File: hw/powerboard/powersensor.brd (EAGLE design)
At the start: 26.3 x 31.1 mm, 35 parts, among them J1 ISP, J2 I2C

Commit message: Added optional I2C pullups, broke out PB0/1 and performed some cosmetical changes to PowerSensor board
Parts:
- added R17, R18: (no value), SparkFun-Passives:0603-RES
- J8: device SparkFun-Connectors:1X04 -> SparkFun-Connectors:1X06
- R1: value (none) -> 12k9
- R10, R11, R2, R5, R8: value (none) -> 1k1
- R4: value (none) -> 4k9
- R7: value (none) -> 2k9
- moved C5 0.16 mm to (8.57, 5.87)
- moved J2 0.16 mm to (1.43, 10.8)
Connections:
- new net PB0: J8.5, U$1.2
- new net PB1: J8.4, U$1.3
- net SCK: now also R17.2
- net SDA/MOSI: now also R18.1
- net VIN: now also J8.6, R17.1, R18.2; no longer J8.4
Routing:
- net PB0: track 0.00 -> 5.35 mm
- net PB1: track 0.00 -> 4.82 mm
- net SDA/MOSI: track 21.3 -> 24.4 mm
- net SCK: track 18.8 -> 21.9 mm
- net VIN: track 29.6 -> 31.8 mm
- net MISO/1.8V_ADC: track 10.1 -> 10.7 mm
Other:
- board text added: "I2C pullups"
- board text added: "MISO"
- board text added: "MOSI"
- board text added: "PB0"
- board text added: "PB1"
- board text added: "PowerSensor v0.1"
- board text added: "RST"
- board text removed: "BIVAC PowerSensor v0.1"

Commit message: Added values and performed some cosmetic changes on PowerSensor schematics
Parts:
- C1, C2, C3, C4: value (none) -> 10u
- R1: value 12k9 -> 13k
- R12, R3, R6, R9: value (none) -> 750R
- R17, R18: value (none) -> 4k7
- R4: value 4k9 -> 4k87
- R7: value 2k9 -> 2k87
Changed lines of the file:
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@@
 </autorouter>
 <elements>
-<element name="C1" library="SparkFun-Capacitors" package="0603-CAP" value="" x="8.89" y="17.78" rot="R90"/>
-<element name="C2" library="SparkFun-Capacitors" package="0603-CAP" value="" x="13.97" y="17.78" rot="R90"/>
-<element name="C3" library="SparkFun-Capacitors" package="0603-CAP" value="" x="19.05" y="17.78" rot="R90"/>
-<element name="C4" library="SparkFun-Capacitors" package="0603-CAP" value="" x="24.13" y="17.78" rot="R90"/>
+<element name="C1" library="SparkFun-Capacitors" package="0603-CAP" value="10u" x="8.89" y="17.78" rot="R90"/>
+<element name="C2" library="SparkFun-Capacitors" package="0603-CAP" value="10u" x="13.97" y="17.78" rot="R90"/>
+<element name="C3" library="SparkFun-Capacitors" package="0603-CAP" value="10u" x="19.05" y="17.78" rot="R90"/>
+<element name="C4" library="SparkFun-Capacitors" package="0603-CAP" value="10u" x="24.13" y="17.78" rot="R90"/>
 <element name="C5" library="SparkFun-Capacitors" package="0603-CAP" value="100nF" x="8.5725" y="5.87375" smashed="yes" rot="R180">
 <attribute name="NAME" x="10.12825" y="6.2865" size="0.4064" layer="25" font="vector" rot="R270"/>
@@
 <attribute name="VALUE" x="18.415" y="29.845" size="1.27" layer="27" rot="R270"/>
 </element>
-<element name="R1" library="SparkFun-Passives" package="0603-RES" value="12k9" x="6.35" y="21.59" rot="R90"/>
+<element name="R1" library="SparkFun-Passives" package="0603-RES" value="13k" x="6.35" y="21.59" rot="R90"/>
 <element name="R10" library="SparkFun-Passives" package="0603-RES" value="1k1" x="21.59" y="21.59" rot="R90"/>
 <element name="R11" library="SparkFun-Passives" package="0603-RES" value="1k1" x="24.13" y="21.59" rot="R270"/>
-<element name="R12" library="SparkFun-Passives" package="0603-RES" value="" x="21.59" y="17.78" rot="R90"/>
+<element name="R12" library="SparkFun-Passives" package="0603-RES" value="750R" x="21.59" y="17.78" rot="R90"/>
 <element name="R13" library="SparkFun-Passives" package="0603-RES" value="" x="8.89" y="28.575" smashed="yes" rot="R270">
 <attribute name="NAME" x="9.4615" y="30.6705" size="0.4064" layer="25" font="vector" rot="R180"/>
@@
 </element>
 <element name="R2" library="SparkFun-Passives" package="0603-RES" value="1k1" x="8.89" y="21.59" rot="R270"/>
-<element name="R3" library="SparkFun-Passives" package="0603-RES" value="" x="6.35" y="17.78" rot="R90"/>
-<element name="R4" library="SparkFun-Passives" package="0603-RES" value="4k9" x="11.43" y="21.59" smashed="yes" rot="R90">
+<element name="R3" library="SparkFun-Passives" package="0603-RES" value="750R" x="6.35" y="17.78" rot="R90"/>
+<element name="R4" library="SparkFun-Passives" package="0603-RES" value="4k87" x="11.43" y="21.59" smashed="yes" rot="R90">
 <attribute name="NAME" x="10.668" y="20.701" size="0.4064" layer="25" font="vector" rot="R90"/>
 <attribute name="VALUE" x="12.573" y="20.574" size="0.4064" layer="27" font="vector" rot="R90"/>
 </element>
 <element name="R5" library="SparkFun-Passives" package="0603-RES" value="1k1" x="13.97" y="21.59" rot="R270"/>
-<element name="R6" library="SparkFun-Passives" package="0603-RES" value="" x="11.43" y="17.78" rot="R90"/>
-<element name="R7" library="SparkFun-Passives" package="0603-RES" value="2k9" x="16.51" y="21.59" rot="R90"/>
+<element name="R6" library="SparkFun-Passives" package="0603-RES" value="750R" x="11.43" y="17.78" rot="R90"/>
+<element name="R7" library="SparkFun-Passives" package="0603-RES" value="2k87" x="16.51" y="21.59" rot="R90"/>
 <element name="R8" library="SparkFun-Passives" package="0603-RES" value="1k1" x="19.05" y="21.59" rot="R270"/>
-<element name="R9" library="SparkFun-Passives" package="0603-RES" value="" x="16.51" y="17.78" rot="R90"/>
+<element name="R9" library="SparkFun-Passives" package="0603-RES" value="750R" x="16.51" y="17.78" rot="R90"/>
 <element name="U$1" library="SparkFun-DigitalIC" package="SO14" value="ATTINY84" x="13.335" y="10.795" smashed="yes">
 <attribute name="PROD_ID" value="IC-11285" x="13.335" y="10.795" size="1.778" layer="27" display="off"/>
@@
 <attribute name="VALUE" x="1.905" y="0" size="1.27" layer="27"/>
 </element>
-<element name="R17" library="SparkFun-Passives" package="0603-RES" value="" x="9.04875" y="10.795" rot="MR0"/>
-<element name="R18" library="SparkFun-Passives" package="0603-RES" value="" x="9.04875" y="8.255" rot="MR180"/>
+<element name="R17" library="SparkFun-Passives" package="0603-RES" value="4k7" x="9.04875" y="10.795" rot="MR0"/>
+<element name="R18" library="SparkFun-Passives" package="0603-RES" value="4k7" x="9.04875" y="8.255" rot="MR180"/>
 </elements>
 <signals>

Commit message: Fixed values and added product ids for PowerSensor BOM
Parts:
- R13: value (none) -> 560R
- R14: value (none) -> 180R
- R15: value (none) -> 82R
- R16: value (none) -> 0R
- R4: value 4k87 -> 4k7
- R7: value 2k87 -> 2k7
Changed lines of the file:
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@@
 <element name="R11" library="SparkFun-Passives" package="0603-RES" value="1k1" x="24.13" y="21.59" rot="R270"/>
 <element name="R12" library="SparkFun-Passives" package="0603-RES" value="750R" x="21.59" y="17.78" rot="R90"/>
-<element name="R13" library="SparkFun-Passives" package="0603-RES" value="" x="8.89" y="28.575" smashed="yes" rot="R270">
+<element name="R13" library="SparkFun-Passives" package="0603-RES" value="560R" x="8.89" y="28.575" smashed="yes" rot="R270">
 <attribute name="NAME" x="9.4615" y="30.6705" size="0.4064" layer="25" font="vector" rot="R180"/>
 <attribute name="VALUE" x="7.747" y="29.591" size="0.4064" layer="27" font="vector" rot="R270"/>
 </element>
-<element name="R14" library="SparkFun-Passives" package="0603-RES" value="" x="13.97" y="28.575" smashed="yes" rot="R270">
+<element name="R14" library="SparkFun-Passives" package="0603-RES" value="180R" x="13.97" y="28.575" smashed="yes" rot="R270">
 <attribute name="NAME" x="14.5415" y="30.6705" size="0.4064" layer="25" font="vector" rot="R180"/>
 <attribute name="VALUE" x="12.827" y="29.591" size="0.4064" layer="27" font="vector" rot="R270"/>
 </element>
-<element name="R15" library="SparkFun-Passives" package="0603-RES" value="" x="19.05" y="28.575" smashed="yes" rot="R270">
+<element name="R15" library="SparkFun-Passives" package="0603-RES" value="82R" x="19.05" y="28.575" smashed="yes" rot="R270">
 <attribute name="NAME" x="19.6215" y="30.6705" size="0.4064" layer="25" font="vector" rot="R180"/>
 <attribute name="VALUE" x="17.907" y="29.591" size="0.4064" layer="27" font="vector" rot="R270"/>
 </element>
-<element name="R16" library="SparkFun-Passives" package="0603-RES" value="" x="24.13" y="28.575" smashed="yes" rot="R270">
+<element name="R16" library="SparkFun-Passives" package="0603-RES" value="0R" x="24.13" y="28.575" smashed="yes" rot="R270">
 <attribute name="NAME" x="24.7015" y="30.6705" size="0.4064" layer="25" font="vector" rot="R180"/>
 <attribute name="VALUE" x="22.987" y="29.591" size="0.4064" layer="27" font="vector" rot="R270"/>
@@
 <element name="R2" library="SparkFun-Passives" package="0603-RES" value="1k1" x="8.89" y="21.59" rot="R270"/>
 <element name="R3" library="SparkFun-Passives" package="0603-RES" value="750R" x="6.35" y="17.78" rot="R90"/>
-<element name="R4" library="SparkFun-Passives" package="0603-RES" value="4k87" x="11.43" y="21.59" smashed="yes" rot="R90">
+<element name="R4" library="SparkFun-Passives" package="0603-RES" value="4k7" x="11.43" y="21.59" smashed="yes" rot="R90">
 <attribute name="NAME" x="10.668" y="20.701" size="0.4064" layer="25" font="vector" rot="R90"/>
 <attribute name="VALUE" x="12.573" y="20.574" size="0.4064" layer="27" font="vector" rot="R90"/>
@@
 <element name="R5" library="SparkFun-Passives" package="0603-RES" value="1k1" x="13.97" y="21.59" rot="R270"/>
 <element name="R6" library="SparkFun-Passives" package="0603-RES" value="750R" x="11.43" y="17.78" rot="R90"/>
-<element name="R7" library="SparkFun-Passives" package="0603-RES" value="2k87" x="16.51" y="21.59" rot="R90"/>
+<element name="R7" library="SparkFun-Passives" package="0603-RES" value="2k7" x="16.51" y="21.59" rot="R90"/>
 <element name="R8" library="SparkFun-Passives" package="0603-RES" value="1k1" x="19.05" y="21.59" rot="R270"/>
 <element name="R9" library="SparkFun-Passives" package="0603-RES" value="750R" x="16.51" y="17.78" rot="R90"/>

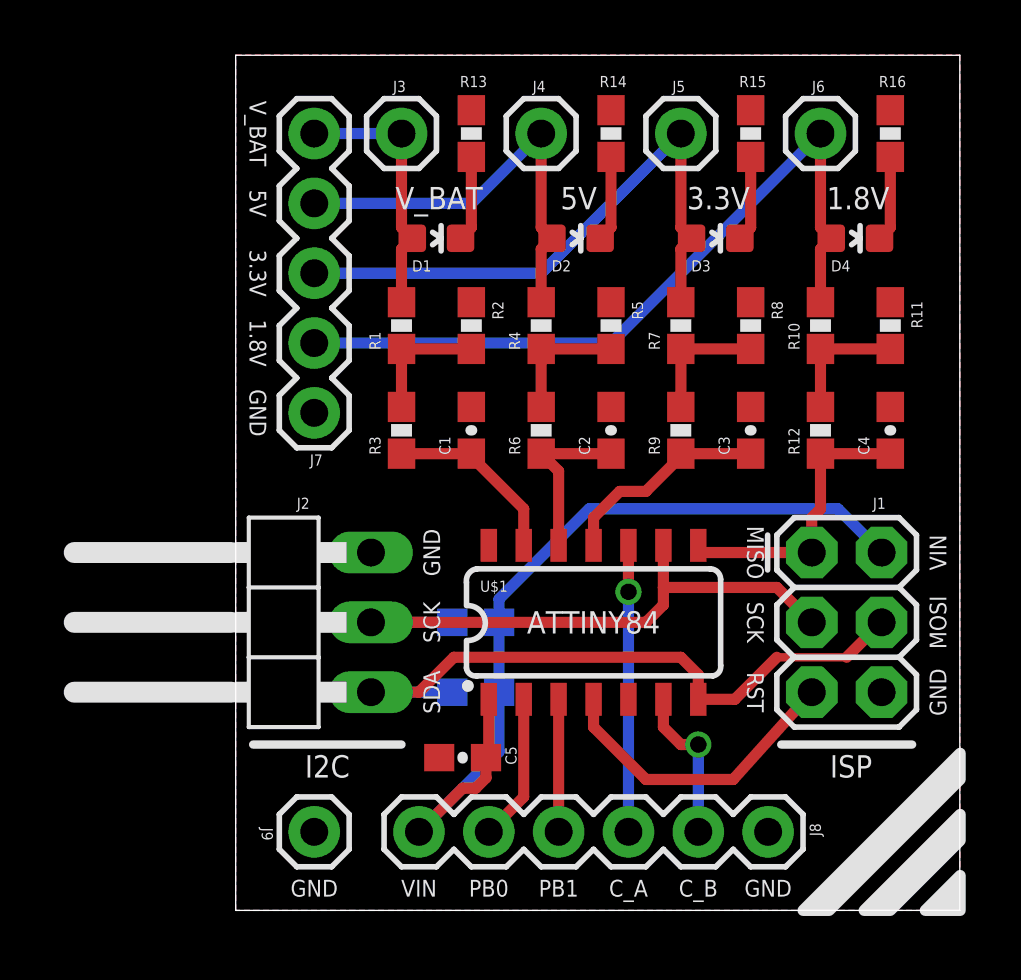
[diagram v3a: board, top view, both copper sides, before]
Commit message: Added PowerSensor package to custom library
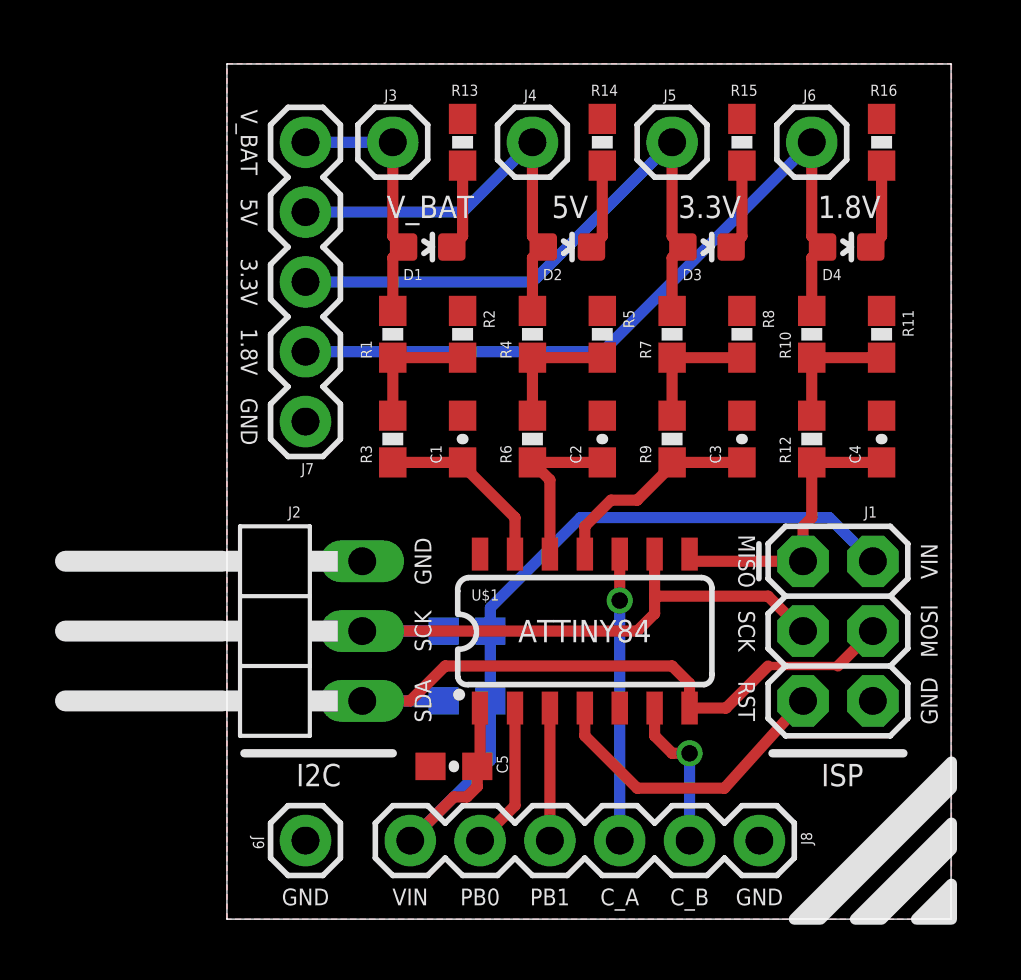
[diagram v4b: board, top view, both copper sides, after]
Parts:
- moved R9 0.45 mm to (16.2, 17.5)
- moved C1 0.45 mm to (8.57, 17.5)
- moved C2 0.45 mm to (13.7, 17.5)
- moved J1 0.45 mm to (21.0, 13.0)
- moved R3 0.45 mm to (6.03, 17.5)
- moved R17 0.45 mm to (8.73, 10.5)
- moved R18 0.45 mm to (8.73, 7.94)
- moved U$1 0.45 mm to (13.0, 10.5)
- moved C3 0.45 mm to (18.7, 17.5)
- moved C4 0.45 mm to (23.8, 17.5)
- moved D3 0.45 mm to (17.5, 24.4)
- moved J5 0.45 mm to (16.2, 28.3)
- moved R12 0.45 mm to (21.3, 17.5)
- moved R6 0.45 mm to (11.1, 17.5)
- moved R7 0.45 mm to (16.2, 21.3)
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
